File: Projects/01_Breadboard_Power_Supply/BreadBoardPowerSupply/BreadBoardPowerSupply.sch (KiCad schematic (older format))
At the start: 0 parts

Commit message: Add parts from parts.md to Eeschema
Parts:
- added C?: 47 μF, symbol Device:CP
- added C?: 470 μF, symbol Device:CP
- added D? (x2): LED, symbol Device:LED
- added D? (x4): 1N4007, Diode_THT:D_DO-41_SOD81_P10.16mm_Horizontal, symbol Diode:1N4007
- added J? (x2): Conn_02x02_Odd_Even, symbol Connector_Generic:Conn_02x02_Odd_Even
- added J?: Barrel_Jack_Switch, symbol Connector:Barrel_Jack_Switch
- added R? (x2): 560 Ω, symbol Device:R
- added SW?: SW_DPDT_x2, symbol Switch:SW_DPDT_x2
- added U?: LM7805_TO220, Package_TO_SOT_THT:TO-220-3_Vertical, symbol Regulator_Linear:LM7805_TO220
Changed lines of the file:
@@
 Comment4 ""
 $EndDescr
+$Comp
+L Device:CP C?
+U 1 1 61CCC3FF
+P 4100 3750
+F 0 "C?" H 4218 3796 50  0000 L CNN
+F 1 "47 μF" H 4218 3705 50  0000 L CNN
+F 2 "" H 4138 3600 50  0001 C CNN
+F 3 "~" H 4100 3750 50  0001 C CNN
+	1    4100 3750
+	1    0    0    -1
+$EndComp
+$Comp
+L Device:CP C?
+U 1 1 61CCDCC0
+P 4100 4150
+F 0 "C?" H 4218 4196 50  0000 L CNN
+F 1 "470 μF" H 4218 4105 50  0000 L CNN
+F 2 "" H 4138 4000 50  0001 C CNN
+F 3 "~" H 4100 4150 50  0001 C CNN
+	1    4100 4150
+	1    0    0    -1
+$EndComp
+$Comp
+L Device:R R?
+U 1 1 61CCEDC9
+P 4800 4400
+F 0 "R?" V 4593 4400 50  0000 C CNN
+F 1 "560 Ω" V 4684 4400 50  0000 C CNN
+F 2 "" V 4730 4400 50  0001 C CNN
+F 3 "~" H 4800 4400 50  0001 C CNN
+	1    4800 4400
+	0    1    1    0
+$EndComp
+$Comp
+L Regulator_Linear:LM7805_TO220 U?
+U 1 1 61CD1970
+P 4800 3850
+F 0 "U?" H 4800 4092 50  0000 C CNN
+F 1 "LM7805_TO220" H 4800 4001 50  0000 C CNN
+F 2 "Package_TO_SOT_THT:TO-220-3_Vertical" H 4800 4075 50  0001 C CIN
+F 3 "https://www.onsemi.cn/PowerSolutions/document/MC7800-D.PDF" H 4800 3800 50  0001 C CNN
+	1    4800 3850
+	1    0    0    -1
+$EndComp
+$Comp
+L Device:LED D?
+U 1 1 61CD6604
+P 4100 4950
+F 0 "D?" H 4093 5167 50  0000 C CNN
+F 1 "LED" H 4093 5076 50  0000 C CNN
+F 2 "" H 4100 4950 50  0001 C CNN
+F 3 "~" H 4100 4950 50  0001 C CNN
+	1    4100 4950
+	1    0    0    -1
+$EndComp
+$Comp
+L Device:LED D?
+U 1 1 61CD7353
+P 4100 4600
+F 0 "D?" H 4093 4817 50  0000 C CNN
+F 1 "LED" H 4093 4726 50  0000 C CNN
+F 2 "" H 4100 4600 50  0001 C CNN
+F 3 "~" H 4100 4600 50  0001 C CNN
+	1    4100 4600
+	1    0    0    -1
+$EndComp
+$Comp
+L Diode:1N4007 D?
+U 1 1 61CD7EFA
+P 5650 4950
+F 0 "D?" H 5650 5167 50  0000 C CNN
+F 1 "1N4007" H 5650 5076 50  0000 C CNN
+F 2 "Diode_THT:D_DO-41_SOD81_P10.16mm_Horizontal" H 5650 4775 50  0001 C CNN
+F 3 "http://www.vishay.com/docs/88503/1n4001.pdf" H 5650 4950 50  0001 C CNN
+	1    5650 4950
+	1    0    0    -1
+$EndComp
+$Comp
+L Diode:1N4007 D?
+U 1 1 61CD92BE
+P 5650 4550
+F 0 "D?" H 5650 4767 50  0000 C CNN
+F 1 "1N4007" H 5650 4676 50  0000 C CNN
+F 2 "Diode_THT:D_DO-41_SOD81_P10.16mm_Horizontal" H 5650 4375 50  0001 C CNN
+F 3 "http://www.vishay.com/docs/88503/1n4001.pdf" H 5650 4550 50  0001 C CNN
+	1    5650 4550
+	1    0    0    -1
+$EndComp
+$Comp
+L Diode:1N4007 D?
+U 1 1 61CD9897
+P 5650 4200
+F 0 "D?" H 5650 4417 50  0000 C CNN
+F 1 "1N4007" H 5650 4326 50  0000 C CNN
+F 2 "Diode_THT:D_DO-41_SOD81_P10.16mm_Horizontal" H 5650 4025 50  0001 C CNN
+F 3 "http://www.vishay.com/docs/88503/1n4001.pdf" H 5650 4200 50  0001 C CNN
+	1    5650 4200
+	1    0    0    -1
+$EndComp
+$Comp
+L Diode:1N4007 D?
+U 1 1 61CDA154
+P 5650 3800
+F 0 "D?" H 5650 4017 50  0000 C CNN
+F 1 "1N4007" H 5650 3926 50  0000 C CNN
+F 2 "Diode_THT:D_DO-41_SOD81_P10.16mm_Horizontal" H 5650 3625 50  0001 C CNN
+F 3 "http://www.vishay.com/docs/88503/1n4001.pdf" H 5650 3800 50  0001 C CNN
+	1    5650 3800
+	1    0    0    -1
+$EndComp
+$Comp
+L Device:R R?
+U 1 1 61CEC084
+P 4800 4700
+F 0 "R?" V 4593 4700 50  0000 C CNN
+F 1 "560 Ω" V 4684 4700 50  0000 C CNN
+F 2 "" V 4730 4700 50  0001 C CNN
+F 3 "~" H 4800 4700 50  0001 C CNN
+	1    4800 4700
+	0    1    1    0
+$EndComp
+$Comp
+L Switch:SW_DPDT_x2 SW?
+U 1 1 61CF1C96
+P 6250 3800
+F 0 "SW?" H 6250 4085 50  0000 C CNN
+F 1 "SW_DPDT_x2" H 6250 3994 50  0000 C CNN
+F 2 "" H 6250 3800 50  0001 C CNN
+F 3 "~" H 6250 3800 50  0001 C CNN
+	1    6250 3800
+	1    0    0    -1
+$EndComp
+$Comp
+L Connector_Generic:Conn_02x02_Odd_Even J?
+U 1 1 61D053F5
+P 6200 4250
+F 0 "J?" H 6250 4467 50  0000 C CNN
+F 1 "Conn_02x02_Odd_Even" H 6250 4376 50  0000 C CNN
+F 2 "" H 6200 4250 50  0001 C CNN
+F 3 "~" H 6200 4250 50  0001 C CNN
+	1    6200 4250
+	1    0    0    -1
+$EndComp
+$Comp
+L Connector_Generic:Conn_02x02_Odd_Even J?
+U 1 1 61D070CC
+P 6200 4650
+F 0 "J?" H 6250 4867 50  0000 C CNN
+F 1 "Conn_02x02_Odd_Even" H 6250 4776 50  0000 C CNN
+F 2 "" H 6200 4650 50  0001 C CNN
+F 3 "~" H 6200 4650 50  0001 C CNN
+	1    6200 4650
+	1    0    0    -1
+$EndComp
+$Comp
+L Connector:Barrel_Jack_Switch J?
+U 1 1 61D0A65C
+P 4800 5250
+F 0 "J?" H 4857 5567 50  0000 C CNN
+F 1 "Barrel_Jack_Switch" H 4857 5476 50  0000 C CNN
+F 2 "" H 4850 5210 50  0001 C CNN
+F 3 "~" H 4850 5210 50  0001 C CNN
+	1    4800 5250
+	1    0    0    -1
+$EndComp
 $EndSCHEMATC

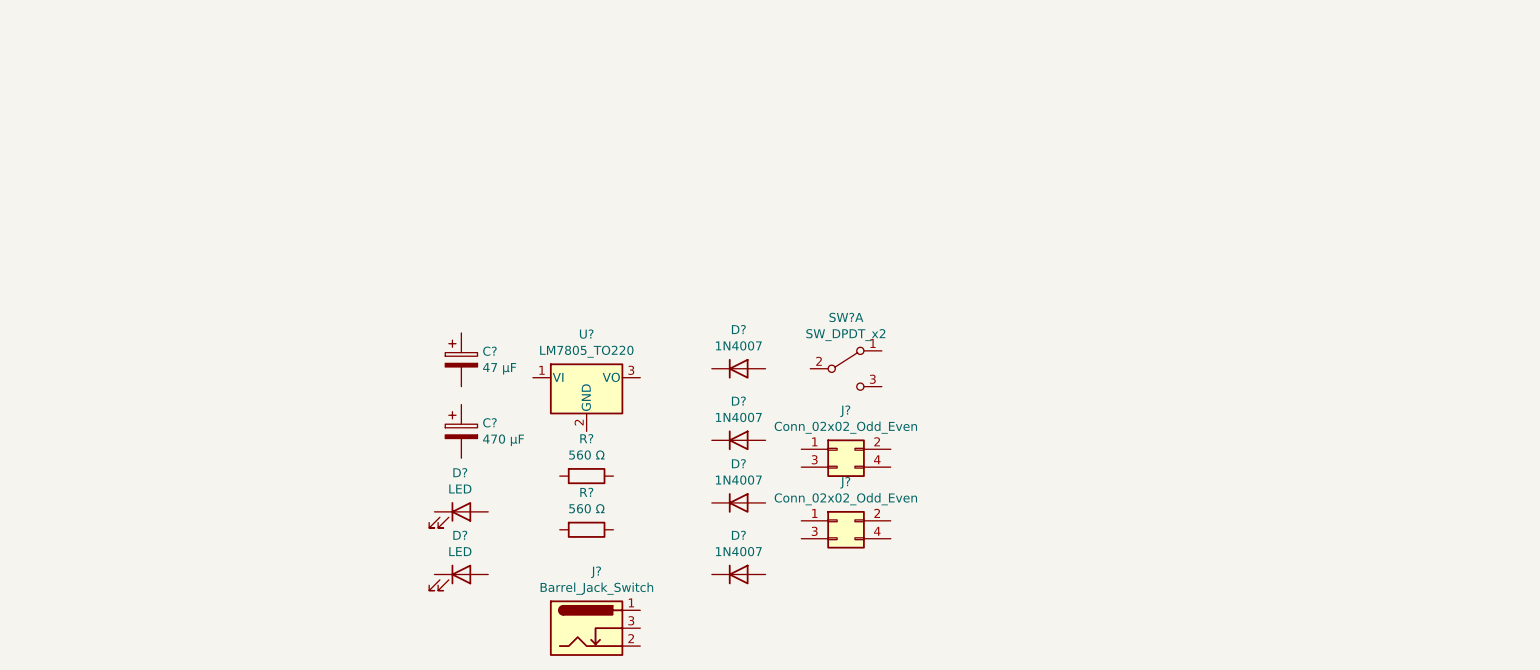
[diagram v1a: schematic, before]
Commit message: Arrange and annotate Eeschema
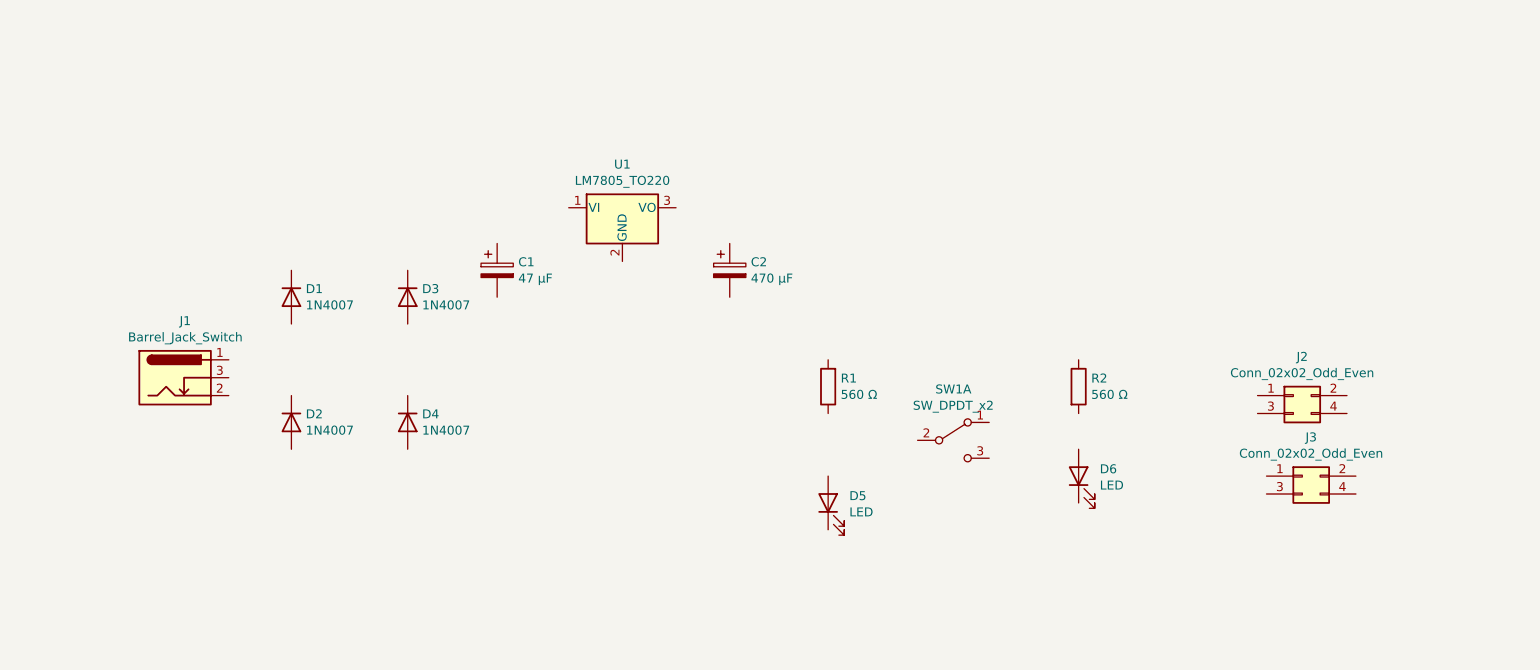
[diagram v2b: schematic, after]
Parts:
- gave numbers to parts that had none: 15
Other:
- moved on the sheet: C1, C2, D1, D2, D3, D4, D5, D6, J1, J2, J3, R1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
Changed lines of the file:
@@
 $EndDescr
 $Comp
-L Device:CP C?
+L Device:CP C1
 U 1 1 61CCC3FF
-P 4100 3750
-F 0 "C?" H 4218 3796 50  0000 L CNN
-F 1 "47 μF" H 4218 3705 50  0000 L CNN
-F 2 "" H 4138 3600 50  0001 C CNN
-F 3 "~" H 4100 3750 50  0001 C CNN
-	1    4100 3750
+P 4300 3250
+F 0 "C1" H 4418 3296 50  0000 L CNN
+F 1 "47 μF" H 4418 3205 50  0000 L CNN
+F 2 "" H 4338 3100 50  0001 C CNN
+F 3 "~" H 4300 3250 50  0001 C CNN
+	1    4300 3250
 	1    0    0    -1
 $EndComp
 $Comp
-L Device:CP C?
+L Device:CP C2
 U 1 1 61CCDCC0
-P 4100 4150
-F 0 "C?" H 4218 4196 50  0000 L CNN
-F 1 "470 μF" H 4218 4105 50  0000 L CNN
-F 2 "" H 4138 4000 50  0001 C CNN
-F 3 "~" H 4100 4150 50  0001 C CNN
-	1    4100 4150
+P 5600 3250
+F 0 "C2" H 5718 3296 50  0000 L CNN
+F 1 "470 μF" H 5718 3205 50  0000 L CNN
+F 2 "" H 5638 3100 50  0001 C CNN
+F 3 "~" H 5600 3250 50  0001 C CNN
+	1    5600 3250
 	1    0    0    -1
 $EndComp
 $Comp
-L Device:R R?
+L Device:R R2
 U 1 1 61CCEDC9
-P 4800 4400
-F 0 "R?" V 4593 4400 50  0000 C CNN
-F 1 "560 Ω" V 4684 4400 50  0000 C CNN
-F 2 "" V 4730 4400 50  0001 C CNN
-F 3 "~" H 4800 4400 50  0001 C CNN
-	1    4800 4400
+P 7550 3900
+F 0 "R2" H 7620 3946 50  0000 L CNN
+F 1 "560 Ω" H 7620 3855 50  0000 L CNN
+F 2 "" V 7480 3900 50  0001 C CNN
+F 3 "~" H 7550 3900 50  0001 C CNN
+	1    7550 3900
+	1    0    0    -1
+$EndComp
+$Comp
+L Regulator_Linear:LM7805_TO220 U1
+U 1 1 61CD1970
+P 5000 2900
+F 0 "U1" H 5000 3142 50  0000 C CNN
+F 1 "LM7805_TO220" H 5000 3051 50  0000 C CNN
+F 2 "Package_TO_SOT_THT:TO-220-3_Vertical" H 5000 3125 50  0001 C CIN
+F 3 "https://www.onsemi.cn/PowerSolutions/document/MC7800-D.PDF" H 5000 2850 50  0001 C CNN
+	1    5000 2900
+	1    0    0    -1
+$EndComp
+$Comp
+L Device:LED D5
+U 1 1 61CD6604
+P 6150 4550
+F 0 "D5" V 6189 4432 50  0000 R CNN
+F 1 "LED" V 6098 4432 50  0000 R CNN
+F 2 "" H 6150 4550 50  0001 C CNN
+F 3 "~" H 6150 4550 50  0001 C CNN
+	1    6150 4550
+	0    -1   -1   0
+$EndComp
+$Comp
+L Device:LED D6
+U 1 1 61CD7353
+P 7550 4400
+F 0 "D6" V 7589 4282 50  0000 R CNN
+F 1 "LED" V 7498 4282 50  0000 R CNN
+F 2 "" H 7550 4400 50  0001 C CNN
+F 3 "~" H 7550 4400 50  0001 C CNN
+	1    7550 4400
+	0    -1   -1   0
+$EndComp
+$Comp
+L Diode:1N4007 D1
+U 1 1 61CD7EFA
+P 3150 3400
+F 0 "D1" V 3104 3480 50  0000 L CNN
+F 1 "1N4007" V 3195 3480 50  0000 L CNN
+F 2 "Diode_THT:D_DO-41_SOD81_P10.16mm_Horizontal" H 3150 3225 50  0001 C CNN
+F 3 "http://www.vishay.com/docs/88503/1n4001.pdf" H 3150 3400 50  0001 C CNN
+	1    3150 3400
 	0    1    1    0
 $EndComp
 $Comp
-L Regulator_Linear:LM7805_TO220 U?
-U 1 1 61CD1970
-P 4800 3850
-F 0 "U?" H 4800 4092 50  0000 C CNN
-F 1 "LM7805_TO220" H 4800 4001 50  0000 C CNN
-F 2 "Package_TO_SOT_THT:TO-220-3_Vertical" H 4800 4075 50  0001 C CIN
-F 3 "https://www.onsemi.cn/PowerSolutions/document/MC7800-D.PDF" H 4800 3800 50  0001 C CNN
-	1    4800 3850
+L Diode:1N4007 D3
+U 1 1 61CD92BE
+P 3800 3400
+F 0 "D3" V 3754 3480 50  0000 L CNN
+F 1 "1N4007" V 3845 3480 50  0000 L CNN
+F 2 "Diode_THT:D_DO-41_SOD81_P10.16mm_Horizontal" H 3800 3225 50  0001 C CNN
+F 3 "http://www.vishay.com/docs/88503/1n4001.pdf" H 3800 3400 50  0001 C CNN
+	1    3800 3400
+	0    1    1    0
+$EndComp
+$Comp
+L Diode:1N4007 D2
+U 1 1 61CD9897
+P 3150 4100
+F 0 "D2" V 3104 4180 50  0000 L CNN
+F 1 "1N4007" V 3195 4180 50  0000 L CNN
+F 2 "Diode_THT:D_DO-41_SOD81_P10.16mm_Horizontal" H 3150 3925 50  0001 C CNN
+F 3 "http://www.vishay.com/docs/88503/1n4001.pdf" H 3150 4100 50  0001 C CNN
+	1    3150 4100
+	0    1    1    0
+$EndComp
+$Comp
+L Diode:1N4007 D4
+U 1 1 61CDA154
+P 3800 4100
+F 0 "D4" V 3754 4180 50  0000 L CNN
+F 1 "1N4007" V 3845 4180 50  0000 L CNN
+F 2 "Diode_THT:D_DO-41_SOD81_P10.16mm_Horizontal" H 3800 3925 50  0001 C CNN
+F 3 "http://www.vishay.com/docs/88503/1n4001.pdf" H 3800 4100 50  0001 C CNN
+	1    3800 4100
+	0    1    1    0
+$EndComp
+$Comp
+L Device:R R1
+U 1 1 61CEC084
+P 6150 3900
+F 0 "R1" H 6080 3854 50  0000 R CNN
+F 1 "560 Ω" H 6080 3945 50  0000 R CNN
+F 2 "" V 6080 3900 50  0001 C CNN
+F 3 "~" H 6150 3900 50  0001 C CNN
+	1    6150 3900
+	-1   0    0    1
+$EndComp
+$Comp
+L Switch:SW_DPDT_x2 SW1
+U 1 1 61CF1C96
+P 6850 4200
+F 0 "SW1" H 6850 4485 50  0000 C CNN
+F 1 "SW_DPDT_x2" H 6850 4394 50  0000 C CNN
+F 2 "" H 6850 4200 50  0001 C CNN
+F 3 "~" H 6850 4200 50  0001 C CNN
+	1    6850 4200
 	1    0    0    -1
 $EndComp
 $Comp
-L Device:LED D?
-U 1 1 61CD6604
-P 4100 4950
-F 0 "D?" H 4093 5167 50  0000 C CNN
-F 1 "LED" H 4093 5076 50  0000 C CNN
-F 2 "" H 4100 4950 50  0001 C CNN
-F 3 "~" H 4100 4950 50  0001 C CNN
-	1    4100 4950
+L Connector_Generic:Conn_02x02_Odd_Even J3
+U 1 1 61D053F5
+P 8800 4400
+F 0 "J3" H 8850 4617 50  0000 C CNN
+F 1 "Conn_02x02_Odd_Even" H 8850 4526 50  0000 C CNN
+F 2 "" H 8800 4400 50  0001 C CNN
+F 3 "~" H 8800 4400 50  0001 C CNN
+	1    8800 4400
 	1    0    0    -1
 $EndComp
 $Comp
-L Device:LED D?
-U 1 1 61CD7353
-P 4100 4600
-F 0 "D?" H 4093 4817 50  0000 C CNN
-F 1 "LED" H 4093 4726 50  0000 C CNN
-F 2 "" H 4100 4600 50  0001 C CNN
-F 3 "~" H 4100 4600 50  0001 C CNN
-	1    4100 4600
+L Connector_Generic:Conn_02x02_Odd_Even J2
+U 1 1 61D070CC
+P 8750 3950
+F 0 "J2" H 8800 4167 50  0000 C CNN
+F 1 "Conn_02x02_Odd_Even" H 8800 4076 50  0000 C CNN
+F 2 "" H 8750 3950 50  0001 C CNN
+F 3 "~" H 8750 3950 50  0001 C CNN
+	1    8750 3950
 	1    0    0    -1
 $EndComp
 $Comp
-L Diode:1N4007 D?
-U 1 1 61CD7EFA
-P 5650 4950
-F 0 "D?" H 5650 5167 50  0000 C CNN
-F 1 "1N4007" H 5650 5076 50  0000 C CNN
-F 2 "Diode_THT:D_DO-41_SOD81_P10.16mm_Horizontal" H 5650 4775 50  0001 C CNN
-F 3 "http://www.vishay.com/docs/88503/1n4001.pdf" H 5650 4950 50  0001 C CNN
-	1    5650 4950
+L Connector:Barrel_Jack_Switch J1
+U 1 1 61D0A65C
+P 2500 3850
+F 0 "J1" H 2557 4167 50  0000 C CNN
+F 1 "Barrel_Jack_Switch" H 2557 4076 50  0000 C CNN
+F 2 "" H 2550 3810 50  0001 C CNN
+F 3 "~" H 2550 3810 50  0001 C CNN
+	1    2500 3850
 	1    0    0    -1
 $EndComp
-$Comp
-L Diode:1N4007 D?
-U 1 1 61CD92BE
-P 5650 4550
-F 0 "D?" H 5650 4767 50  0000 C CNN
-F 1 "1N4007" H 5650 4676 50  0000 C CNN
-F 2 "Diode_THT:D_DO-41_SOD81_P10.16mm_Horizontal" H 5650 4375 50  0001 C CNN
-F 3 "http://www.vishay.com/docs/88503/1n4001.pdf" H 5650 4550 50  0001 C CNN
-	1    5650 4550
-	1    0    0    -1
-$EndComp
-$Comp
-L Diode:1N4007 D?
-U 1 1 61CD9897
-P 5650 4200
-F 0 "D?" H 5650 4417 50  0000 C CNN
-F 1 "1N4007" H 5650 4326 50  0000 C CNN
-F 2 "Diode_THT:D_DO-41_SOD81_P10.16mm_Horizontal" H 5650 4025 50  0001 C CNN
-F 3 "http://www.vishay.com/docs/88503/1n4001.pdf" H 5650 4200 50  0001 C CNN
-	1    5650 4200
-	1    0    0    -1
-$EndComp
-$Comp
-L Diode:1N4007 D?
-U 1 1 61CDA154
-P 5650 3800
-F 0 "D?" H 5650 4017 50  0000 C CNN
-F 1 "1N4007" H 5650 3926 50  0000 C CNN
-F 2 "Diode_THT:D_DO-41_SOD81_P10.16mm_Horizontal" H 5650 3625 50  0001 C CNN
-F 3 "http://www.vishay.com/docs/88503/1n4001.pdf" H 5650 3800 50  0001 C CNN
-	1    5650 3800
-	1    0    0    -1
-$EndComp
-$Comp
-L Device:R R?
-U 1 1 61CEC084
-P 4800 4700
-F 0 "R?" V 4593 4700 50  0000 C CNN
-F 1 "560 Ω" V 4684 4700 50  0000 C CNN
-F 2 "" V 4730 4700 50  0001 C CNN
-F 3 "~" H 4800 4700 50  0001 C CNN
-	1    4800 4700
-	0    1    1    0
-$EndComp
-$Comp
-L Switch:SW_DPDT_x2 SW?
-U 1 1 61CF1C96
-P 6250 3800
-F 0 "SW?" H 6250 4085 50  0000 C CNN
-F 1 "SW_DPDT_x2" H 6250 3994 50  0000 C CNN
-F 2 "" H 6250 3800 50  0001 C CNN
-F 3 "~" H 6250 3800 50  0001 C CNN
-	1    6250 3800
-	1    0    0    -1
-$EndComp
-$Comp
-L Connector_Generic:Conn_02x02_Odd_Even J?
-U 1 1 61D053F5
-P 6200 4250
-F 0 "J?" H 6250 4467 50  0000 C CNN
-F 1 "Conn_02x02_Odd_Even" H 6250 4376 50  0000 C CNN
-F 2 "" H 6200 4250 50  0001 C CNN
-F 3 "~" H 6200 4250 50  0001 C CNN
-	1    6200 4250
-	1    0    0    -1
-$EndComp
-$Comp
-L Connector_Generic:Conn_02x02_Odd_Even J?
-U 1 1 61D070CC
-P 6200 4650
-F 0 "J?" H 6250 4867 50  0000 C CNN
-F 1 "Conn_02x02_Odd_Even" H 6250 4776 50  0000 C CNN
-F 2 "" H 6200 4650 50  0001 C CNN
-F 3 "~" H 6200 4650 50  0001 C CNN
-	1    6200 4650
-	1    0    0    -1
-$EndComp
-$Comp
-L Connector:Barrel_Jack_Switch J?
-U 1 1 61D0A65C
-P 4800 5250
-F 0 "J?" H 4857 5567 50  0000 C CNN
-F 1 "Barrel_Jack_Switch" H 4857 5476 50  0000 C CNN
-F 2 "" H 4850 5210 50  0001 C CNN
-F 3 "~" H 4850 5210 50  0001 C CNN
-	1    4800 5250
-	1    0    0    -1
-$EndComp

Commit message: Assign footprints to all but slide switch - the slide switch likely requires a third party library!
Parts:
- C1: footprint (none) -> Capacitor_THT:CP_Radial_D10.0mm_P5.00mm
- C2: footprint (none) -> Capacitor_THT:CP_Radial_D6.3mm_P2.50mm
- D5, D6: footprint (none) -> LED_THT:LED_D5.0mm
- J1: footprint (none) -> Connector_BarrelJack:BarrelJack_CUI_PJ-102AH_Horizontal
- J2, J3: footprint (none) -> Connector_PinHeader_2.54mm:PinHeader_2x02_P2.54mm_Vertical
- R1, R2: footprint (none) -> Resistor_THT:R_Axial_DIN0207_L6.3mm_D2.5mm_P7.62mm_Horizontal
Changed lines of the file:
@@
 F 0 "C1" H 4418 3296 50  0000 L CNN
 F 1 "47 μF" H 4418 3205 50  0000 L CNN
-F 2 "" H 4338 3100 50  0001 C CNN
+F 2 "Capacitor_THT:CP_Radial_D10.0mm_P5.00mm" H 4338 3100 50  0001 C CNN
 F 3 "~" H 4300 3250 50  0001 C CNN
 	1    4300 3250
@@
 F 0 "C2" H 5718 3296 50  0000 L CNN
 F 1 "470 μF" H 5718 3205 50  0000 L CNN
-F 2 "" H 5638 3100 50  0001 C CNN
+F 2 "Capacitor_THT:CP_Radial_D6.3mm_P2.50mm" H 5638 3100 50  0001 C CNN
 F 3 "~" H 5600 3250 50  0001 C CNN
 	1    5600 3250
@@
 F 0 "R2" H 7620 3946 50  0000 L CNN
 F 1 "560 Ω" H 7620 3855 50  0000 L CNN
-F 2 "" V 7480 3900 50  0001 C CNN
+F 2 "Resistor_THT:R_Axial_DIN0207_L6.3mm_D2.5mm_P7.62mm_Horizontal" V 7480 3900 50  0001 C CNN
 F 3 "~" H 7550 3900 50  0001 C CNN
 	1    7550 3900
@@
 F 0 "D5" V 6189 4432 50  0000 R CNN
 F 1 "LED" V 6098 4432 50  0000 R CNN
-F 2 "" H 6150 4550 50  0001 C CNN
+F 2 "LED_THT:LED_D5.0mm" H 6150 4550 50  0001 C CNN
 F 3 "~" H 6150 4550 50  0001 C CNN
 	1    6150 4550
@@
 F 0 "D6" V 7589 4282 50  0000 R CNN
 F 1 "LED" V 7498 4282 50  0000 R CNN
-F 2 "" H 7550 4400 50  0001 C CNN
+F 2 "LED_THT:LED_D5.0mm" H 7550 4400 50  0001 C CNN
 F 3 "~" H 7550 4400 50  0001 C CNN
 	1    7550 4400
@@
 F 0 "R1" H 6080 3854 50  0000 R CNN
 F 1 "560 Ω" H 6080 3945 50  0000 R CNN
-F 2 "" V 6080 3900 50  0001 C CNN
+F 2 "Resistor_THT:R_Axial_DIN0207_L6.3mm_D2.5mm_P7.62mm_Horizontal" V 6080 3900 50  0001 C CNN
 F 3 "~" H 6150 3900 50  0001 C CNN
 	1    6150 3900
@@
 F 0 "J3" H 8850 4617 50  0000 C CNN
 F 1 "Conn_02x02_Odd_Even" H 8850 4526 50  0000 C CNN
-F 2 "" H 8800 4400 50  0001 C CNN
+F 2 "Connector_PinHeader_2.54mm:PinHeader_2x02_P2.54mm_Vertical" H 8800 4400 50  0001 C CNN
 F 3 "~" H 8800 4400 50  0001 C CNN
 	1    8800 4400
@@
 F 0 "J2" H 8800 4167 50  0000 C CNN
 F 1 "Conn_02x02_Odd_Even" H 8800 4076 50  0000 C CNN
-F 2 "" H 8750 3950 50  0001 C CNN
+F 2 "Connector_PinHeader_2.54mm:PinHeader_2x02_P2.54mm_Vertical" H 8750 3950 50  0001 C CNN
 F 3 "~" H 8750 3950 50  0001 C CNN
 	1    8750 3950
@@
 F 0 "J1" H 2557 4167 50  0000 C CNN
 F 1 "Barrel_Jack_Switch" H 2557 4076 50  0000 C CNN
-F 2 "" H 2550 3810 50  0001 C CNN
+F 2 "Connector_BarrelJack:BarrelJack_CUI_PJ-102AH_Horizontal" H 2550 3810 50  0001 C CNN
 F 3 "~" H 2550 3810 50  0001 C CNN
 	1    2500 3850

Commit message: Associate slide switch footprint with switch from digikey library
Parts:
- SW1: footprint (none) -> digikey-footprints:Switch_Slide_11.6x4mm_EG1218
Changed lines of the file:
@@
 F 0 "SW1" H 6850 4485 50  0000 C CNN
 F 1 "SW_DPDT_x2" H 6850 4394 50  0000 C CNN
-F 2 "" H 6850 4200 50  0001 C CNN
+F 2 "digikey-footprints:Switch_Slide_11.6x4mm_EG1218" H 6850 4200 50  0001 C CNN
 F 3 "~" H 6850 4200 50  0001 C CNN
 	1    6850 4200

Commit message: Wire Eeschema and run ERC
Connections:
- net at C1.1: now also D1.1 (K), D3.1 (K), U1.1 (VI)
- net at C1.2: now also C2.2, D2.2 (A), D4.2 (A), D5.1 (K), D6.1 (K), J2.3 (Pin_3), J2.4 (Pin_4), J3.3 (Pin_3), J3.4 (Pin_4), U1.2 (GND)
- net at C2.1: now also R1.2, SW1.2 (B), U1.3 (VO)
- net at R2.1: now also J2.1 (Pin_1), J2.2 (Pin_2), J3.1 (Pin_1), J3.2 (Pin_2), SW1.1 (A)
- net at R2.2: now also D6.2 (A)
- net at D5.2 (A): now also R1.1
- net at D1.2 (A): now also D2.1 (K), J1.1
- net at D3.2 (A): now also D4.1 (K), J1.2
- no-connect marks 0 -> 2
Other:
- moved on the sheet: C1, C2, D1, D2, D3, D4, D5, D6, J1, J2, J3, R1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

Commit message: Add netlist names and rerun Eeschema
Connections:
- net Vin: now reaches C1.1, D1.1 (K), D3.1 (K), U1.1 (VI)
- net V-: now reaches C1.2, C2.2, D2.2 (A), D4.2 (A), D5.1 (K), D6.1 (K), J2.3 (Pin_3), J2.4 (Pin_4), J3.3 (Pin_3), J3.4 (Pin_4), U1.2 (GND)
- net Vout1: now reaches C2.1, R1.2, SW1.2 (B), U1.3 (VO)
- net Vout2: now reaches J2.1 (Pin_1), J2.2 (Pin_2), J3.1 (Pin_1), J3.2 (Pin_2), R2.1, SW1.1 (A)
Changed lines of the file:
@@
 	0    1    1    0
 $EndComp
-$Comp
-L Connector:Barrel_Jack_Switch J1
-U 1 1 61D0A65C
-P 2300 3350
-F 0 "J1" H 2357 3667 50  0000 C CNN
-F 1 "Barrel_Jack_Switch" H 2357 3576 50  0000 C CNN
-F 2 "Connector_BarrelJack:BarrelJack_CUI_PJ-102AH_Horizontal" H 2350 3310 50  0001 C CNN
-F 3 "~" H 2350 3310 50  0001 C CNN
-	1    2300 3350
-	1    0    0    -1
-$EndComp
 Wire Wire Line
 	2600 3250 2800 3250
@@
 Wire Wire Line
 	2800 3450 2800 3400
-NoConn ~ 2600 3350
 $Comp
 L Diode:1N4007 D2
@@
 	0    -1   -1   0
 $EndComp
+Text Label 3350 2600 0    50   ~ 0
+Vin
+Text Label 3400 4150 0    50   ~ 0
+V-
+Text Label 5200 2600 0    50   ~ 0
+Vout1
+Text Label 7050 2500 0    50   ~ 0
+Vout2
+NoConn ~ 2600 3350
+$Comp
+L Connector:Barrel_Jack_Switch J1
+U 1 1 61D0A65C
+P 2300 3350
+F 0 "J1" H 2357 3667 50  0000 C CNN
+F 1 "Barrel_Jack_Switch" H 2357 3576 50  0000 C CNN
+F 2 "Connector_BarrelJack:BarrelJack_CUI_PJ-102AH_Horizontal" H 2350 3310 50  0001 C CNN
+F 3 "~" H 2350 3310 50  0001 C CNN
+	1    2300 3350
+	1    0    0    -1
+$EndComp
 $EndSCHEMATC
